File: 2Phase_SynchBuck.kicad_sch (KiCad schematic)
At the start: 0 parts

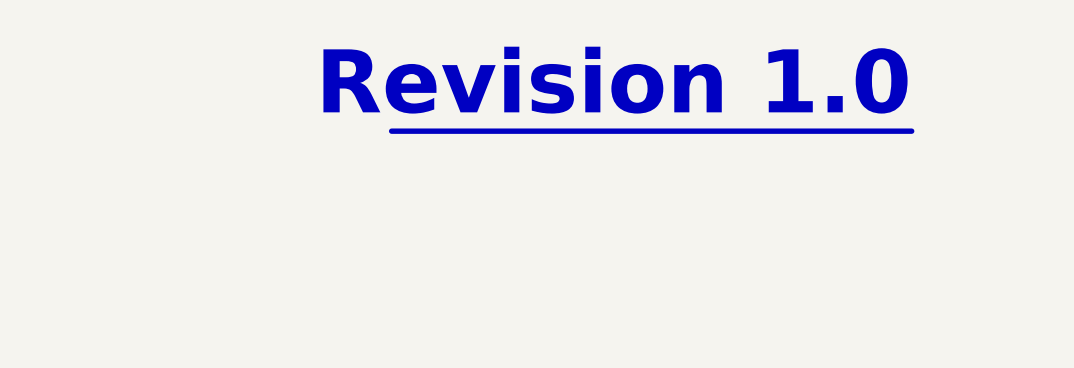
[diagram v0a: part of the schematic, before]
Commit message: Rev1.1
- Removed the Mosfet that Enable the ICs Gate Driver (p.1)
- Changed ADC input Capacitor 47pF to 1nF. (p.6
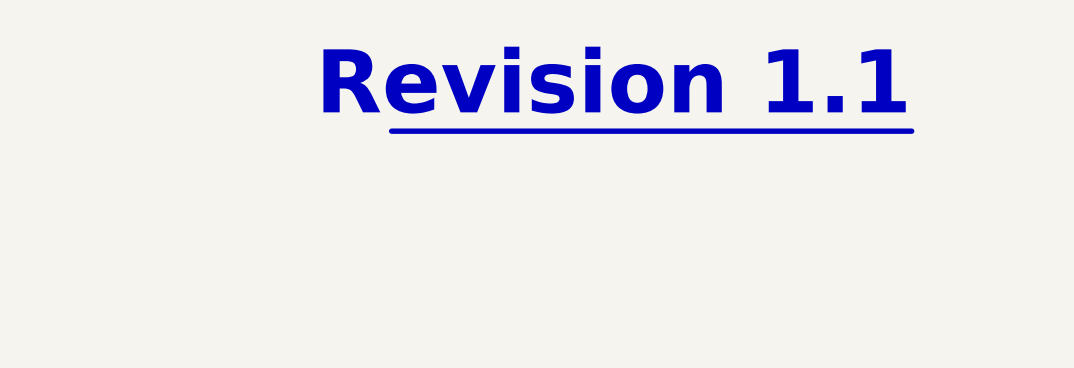
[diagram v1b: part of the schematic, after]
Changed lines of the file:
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@@
 	(paper "A3")
 	(title_block
-		(rev "1.0")
+		(rev "1.1")
 		(comment 1 "Project Overview")
 		(comment 2 "Cover Page")
